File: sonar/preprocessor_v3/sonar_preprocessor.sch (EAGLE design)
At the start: 3 parts

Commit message: Worked on general board dimensions
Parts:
- removed PH1, PH2: PINHD-2X23_2.54, pinhead-1:PINHD-2X23_2.54
- added P8, P9: PINHD-2X23_2.54, pinhead-1:PINHD-2X23_2.54
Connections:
- new net DGND: P9.2

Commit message: Work on headers
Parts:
- removed P8, P9: PINHD-2X23_2.54, pinhead-1:PINHD-2X23_2.54
- added PH1, PH2: PINHD-2X23_2.54, pinhead-1:PINHD-2X23_2.54
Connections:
- removed net DGND: P9.2
- new net AIN0: PH2.39
- new net AIN1: PH2.40
- new net AIN2: PH2.37
- new net AIN3: PH2.38
- new net AIN4: PH2.33
- new net AIN5: PH2.36
- new net AIN6: PH2.35
- new net ECAPWMO: PH2.42
- new net EHRPPWM2A: PH1.19
- new net EHRPWM1A: PH2.14
- new net EHRPWM1B: PH2.16
- new net EHRPWM2B: PH1.13
- new net GND: JP2.1, PH1.1, PH1.2, PH2.1, PH2.2, PH2.43, PH2.44, PH2.45, PH2.46
- new net GND_ADC: PH2.34
- new net GPIO_112: PH2.30
- new net GPIO_115: PH2.27
- new net GPIO_117: PH2.25
- new net GPIO_20: PH2.41
- new net GPIO_26: PH1.14
- new net GPIO_27: PH1.17
- new net GPIO_44: PH1.12
- new net GPIO_45: PH1.11
- new net GPIO_46: PH1.16
- new net GPIO_47: PH1.15
- new net GPIO_48: PH2.15
- new net GPIO_49: PH2.23
- new net GPIO_60: PH2.12
- new net GPIO_61: PH1.26
- new net GPIO_65: PH1.18
- new net GPIO_66: PH1.7
- new net GPIO_67: PH1.8
- new net GPIO_68: PH1.10
- new net GPIO_69: PH1.9
- new net I2C_SCL: PH2.19
- new net I2C_SDA: PH2.20
- new net IN0: JP2.2
- new net IN1: JP2.4
- new net IN2: JP2.6
- new net IN3: JP2.8
- new net IN4: JP2.10
- new net LCD_AC_BIAS: PH1.30
- new net LCD_DATA0: PH1.45
- new net LCD_DATA1: PH1.46
- new net LCD_DATA10: PH1.36
- new net LCD_DATA11: PH1.34
- new net LCD_DATA12: PH1.35
- new net LCD_DATA13: PH1.33
- new net LCD_DATA14: PH1.31
- new net LCD_DATA15: PH1.32
- new net LCD_DATA2: PH1.43
- new net LCD_DATA3: PH1.44
- new net LCD_DATA4: PH1.41
- new net LCD_DATA5: PH1.42
- new net LCD_DATA6: PH1.39
- new net LCD_DATA7: PH1.40
- new net LCD_DATA8: PH1.37
- new net LCD_DATA9: PH1.38
- new net LCD_HSYNC: PH1.29
- new net LCD_PCLK: PH1.28
- new net LCD_VSYNC: PH1.27
- new net MMC1_CLK: PH1.21
- new net MMC1_CMD: PH1.20
- new net MMC1_DAT1: PH1.24
- new net MMC1_DAT2: PH1.5
- new net MMC1_DAT3: PH1.6
- new net MMC1_DAT4: PH1.23
- new net MMC1_DAT5: PH1.22
- new net MMC1_DAT6: PH1.3
- new net MMC1_DAT7: PH1.4
- new net MMC1_DATO: PH1.25
- new net PWR_BUT: PH2.9
- new net SP11_CLK: PH2.31
- new net SP11_CSO: PH2.28
- new net SP11_DO: PH2.29
- new net SPIO_CSO: PH2.17
- new net SPIO_D1: PH2.18
- new net SPIO_DO: PH2.21
- new net SPIO_SCLK: PH2.22
- new net SYS_5V: PH2.7, PH2.8
- new net SYS_RESET: PH2.10
- new net UART1_RXD: PH2.26
- new net UART1_TXD: PH2.24
- new net UART4_RXD: PH2.11
- new net UART4_TXD: PH2.13
- new net VDD_3V3: PH2.3, PH2.4
- new net VDD_5V: PH2.5, PH2.6
- new net VDD_ADC: PH2.32
- new net VREF: JP2.9

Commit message: Reworked board dimensions and mounting
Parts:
- removed JP2: (no value), pinhead:PINHD-2X5
- removed PH1, PH2: PINHD-2X23_2.54, pinhead-1:PINHD-2X23_2.54
- added C1, C3, C5: 100n, rcl:C-EUC0805
- added C10, C8, C9: (no value), Kondensatoren (rev17a):WCAP-AS5H_4X5,5_865230340001
- added C4, C6, C7: 1u, rcl:C-EUC0805
- added CON4: MOLEX_5566-2, ARVP:MOLEX_5566-2
- added JP1: (no value), pinhead:PINHD-1X5/90
- added R1, R10, R11, R2, R5, R6, R7, R8, R9: 25k, rcl:R-US_R0805
- added R3, R4: 10k, rcl:R-US_R0805
- added U1: TEENSY_3.1_BASIC, Teensy_3_Series_Board_v1.0:TEENSY_3.1_BASIC
- added U2: LTC6242, ARVP:LTC6242IGNPBFSSOP16
- added U3: REF3318AIDBZRSOT-23, ARVP:REF3318AIDBZRSOT-23
- added U4: TLV70018DDCRSOT-5, ARVP:TLV70018DDCRSOT-5
- added X1, X2, X3: BN35N61, con-coax:BN35N61
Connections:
- removed net AIN0: PH2.39
- removed net AIN1: PH2.40
- removed net AIN2: PH2.37
- removed net AIN3: PH2.38
- removed net AIN4: PH2.33
- removed net AIN5: PH2.36
- removed net AIN6: PH2.35
- removed net ECAPWMO: PH2.42
- removed net EHRPPWM2A: PH1.19
- removed net EHRPWM1A: PH2.14
- removed net EHRPWM1B: PH2.16
- removed net EHRPWM2B: PH1.13
- removed net GND_ADC: PH2.34
- removed net GPIO_112: PH2.30
- removed net GPIO_115: PH2.27
- removed net GPIO_117: PH2.25
- removed net GPIO_20: PH2.41
- removed net GPIO_26: PH1.14
- removed net GPIO_27: PH1.17
- removed net GPIO_44: PH1.12
- removed net GPIO_45: PH1.11
- removed net GPIO_46: PH1.16
- removed net GPIO_47: PH1.15
- removed net GPIO_48: PH2.15
- removed net GPIO_49: PH2.23
- removed net GPIO_60: PH2.12
- removed net GPIO_61: PH1.26
- removed net GPIO_65: PH1.18
- removed net GPIO_66: PH1.7
- removed net GPIO_67: PH1.8
- removed net GPIO_68: PH1.10
- removed net GPIO_69: PH1.9
- removed net IN0: JP2.2
- removed net IN1: JP2.4
- removed net IN2: JP2.6
- removed net IN3: JP2.8
- removed net IN4: JP2.10
- removed net LCD_AC_BIAS: PH1.30
- removed net LCD_DATA0: PH1.45
- removed net LCD_DATA1: PH1.46
- removed net LCD_DATA10: PH1.36
- removed net LCD_DATA11: PH1.34
- removed net LCD_DATA12: PH1.35
- removed net LCD_DATA13: PH1.33
- removed net LCD_DATA14: PH1.31
- removed net LCD_DATA15: PH1.32
- removed net LCD_DATA2: PH1.43
- removed net LCD_DATA3: PH1.44
- removed net LCD_DATA4: PH1.41
- removed net LCD_DATA5: PH1.42
- removed net LCD_DATA6: PH1.39
- removed net LCD_DATA7: PH1.40
- removed net LCD_DATA8: PH1.37
- removed net LCD_DATA9: PH1.38
- removed net LCD_HSYNC: PH1.29
- removed net LCD_PCLK: PH1.28
- removed net LCD_VSYNC: PH1.27
- removed net MMC1_CLK: PH1.21
- removed net MMC1_CMD: PH1.20
- removed net MMC1_DAT1: PH1.24
- removed net MMC1_DAT2: PH1.5
- removed net MMC1_DAT3: PH1.6
- removed net MMC1_DAT4: PH1.23
- removed net MMC1_DAT5: PH1.22
- removed net MMC1_DAT6: PH1.3
- removed net MMC1_DAT7: PH1.4
- removed net MMC1_DATO: PH1.25
- removed net PWR_BUT: PH2.9
- removed net SP11_CLK: PH2.31
- removed net SP11_CSO: PH2.28
- removed net SP11_DO: PH2.29
- removed net SPIO_CSO: PH2.17
- removed net SPIO_D1: PH2.18
- removed net SPIO_DO: PH2.21
- removed net SPIO_SCLK: PH2.22
- removed net SYS_5V: PH2.7, PH2.8
- removed net SYS_RESET: PH2.10
- removed net UART4_RXD: PH2.11
- removed net UART4_TXD: PH2.13
- removed net VDD_3V3: PH2.3, PH2.4
- removed net VDD_ADC: PH2.32
- removed net VREF: JP2.9
- new net +1V8: C3.1, C4.1, U2.V+, U4.OUT
- new net +3V3: R3.1, R4.1, U1.3.3V
- new net +5V: C1.1, C7.1, CON4G$1.S, U3.VIN, U4.EN, U4.IN
- new net 1V8_REF: C5.1, C6.1, R1.2, R6.2, R9.2, U3.VOUT
- new net BIASED_0: C8.1, R1.1, R2.2, R5.2
- new net BIASED_1: C9.1, R6.1, R7.2, R8.2
- new net BIASED_2: C10.1, R10.2, R11.2, R9.1
- new net CLAMP_IN_0: R5.1, U2.+INC
- new net CLAMP_IN_1: R8.1, U2.+IND
- new net CLAMP_IN_2: R11.1, U2.+INA
- new net FILTER_OUT_0: C8.2
- new net FILTER_OUT_1: C9.2
- new net FILTER_OUT_2: C10.2
- new net SIG_OUT_0: JP1.5, U2.-INC, U2.OUTC
- new net SIG_OUT_1: JP1.3, U2.-IND, U2.OUTD
- new net SIG_OUT_2: JP1.1, U2.-INA, U2.OUTA
- net GND: now also C1.2, C3.2, C4.2, C5.2, C6.2, C7.2, CON4G$2.S, JP1.2, JP1.4, R10.1, R2.1, R7.1, U1.AGND, U1.GND, U2.V-, U3.GND, U4.GND, U4.NC, X1.2, X2.2, X3.2; no longer JP2.1, PH1.1, PH1.2, PH2.1, PH2.2, PH2.43, PH2.44, PH2.45, PH2.46
- net I2C_SCL: now also R4.2, U1.19/A5/T/SCL0; no longer PH2.19
- net I2C_SDA: now also R3.2, U1.18/A4/T/SDA0; no longer PH2.20
- net UART1_RXD: now also U1.0/RX1/T; no longer PH2.26
- net UART1_TXD: now also U1.1/TX1/T; no longer PH2.24
- net VDD_5V: now also U1.VBAT; no longer PH2.5, PH2.6

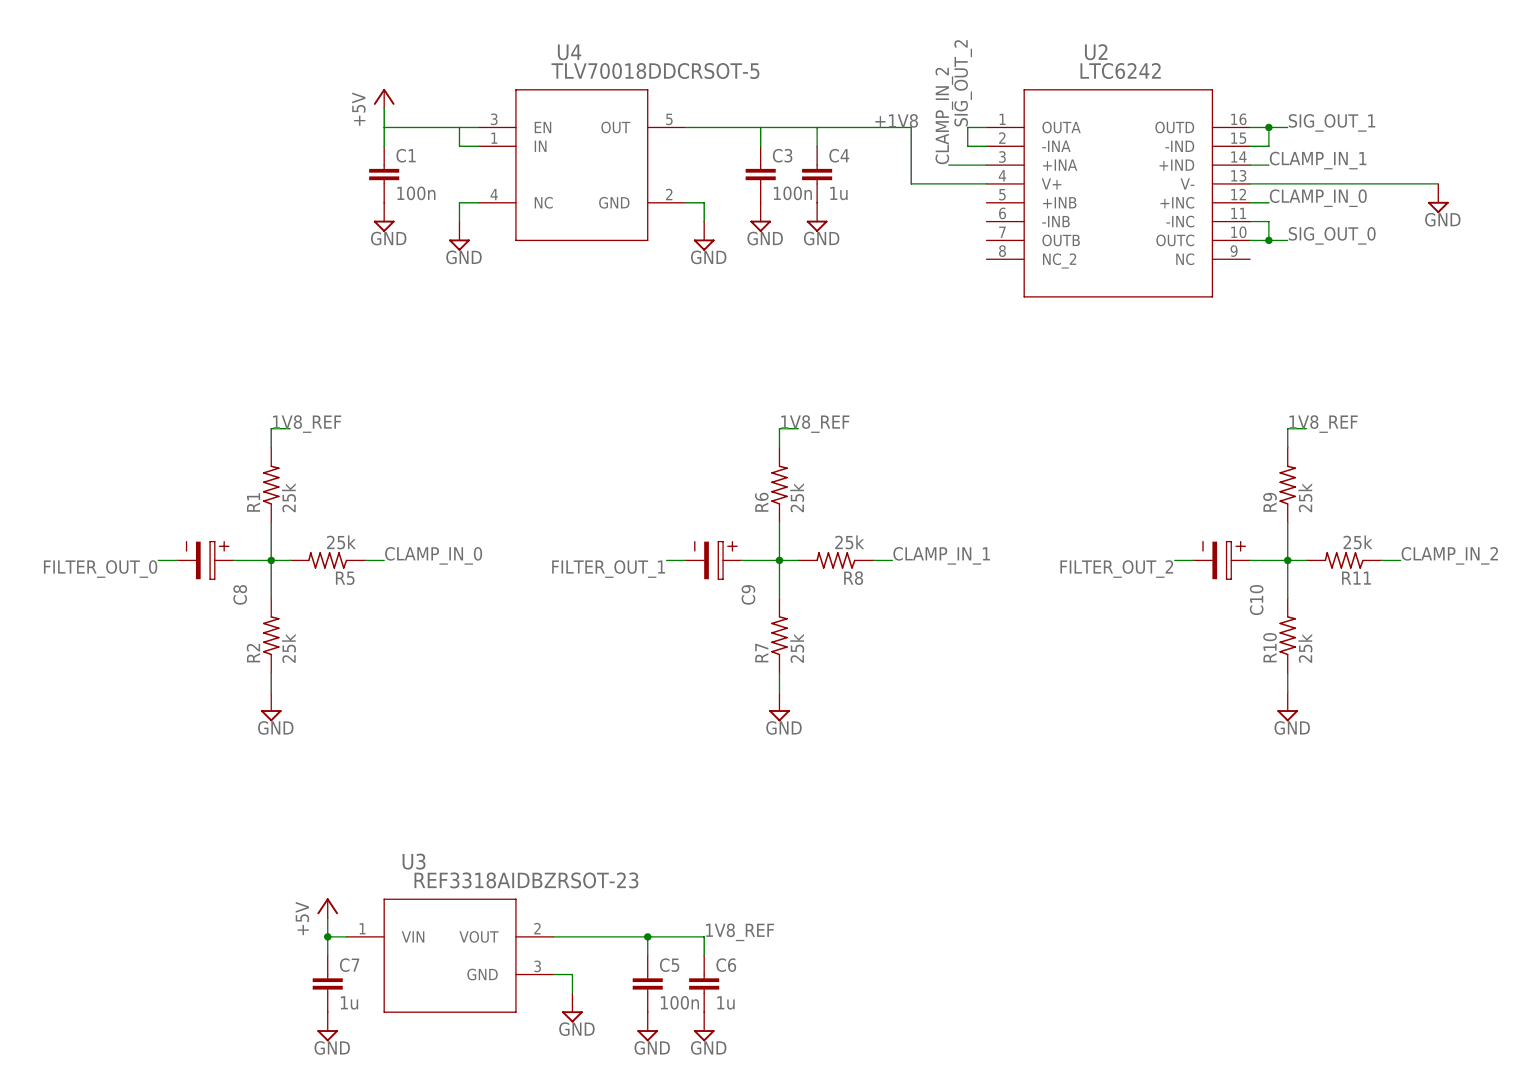
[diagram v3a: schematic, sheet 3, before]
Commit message: Bias/clamp work, overall layout work
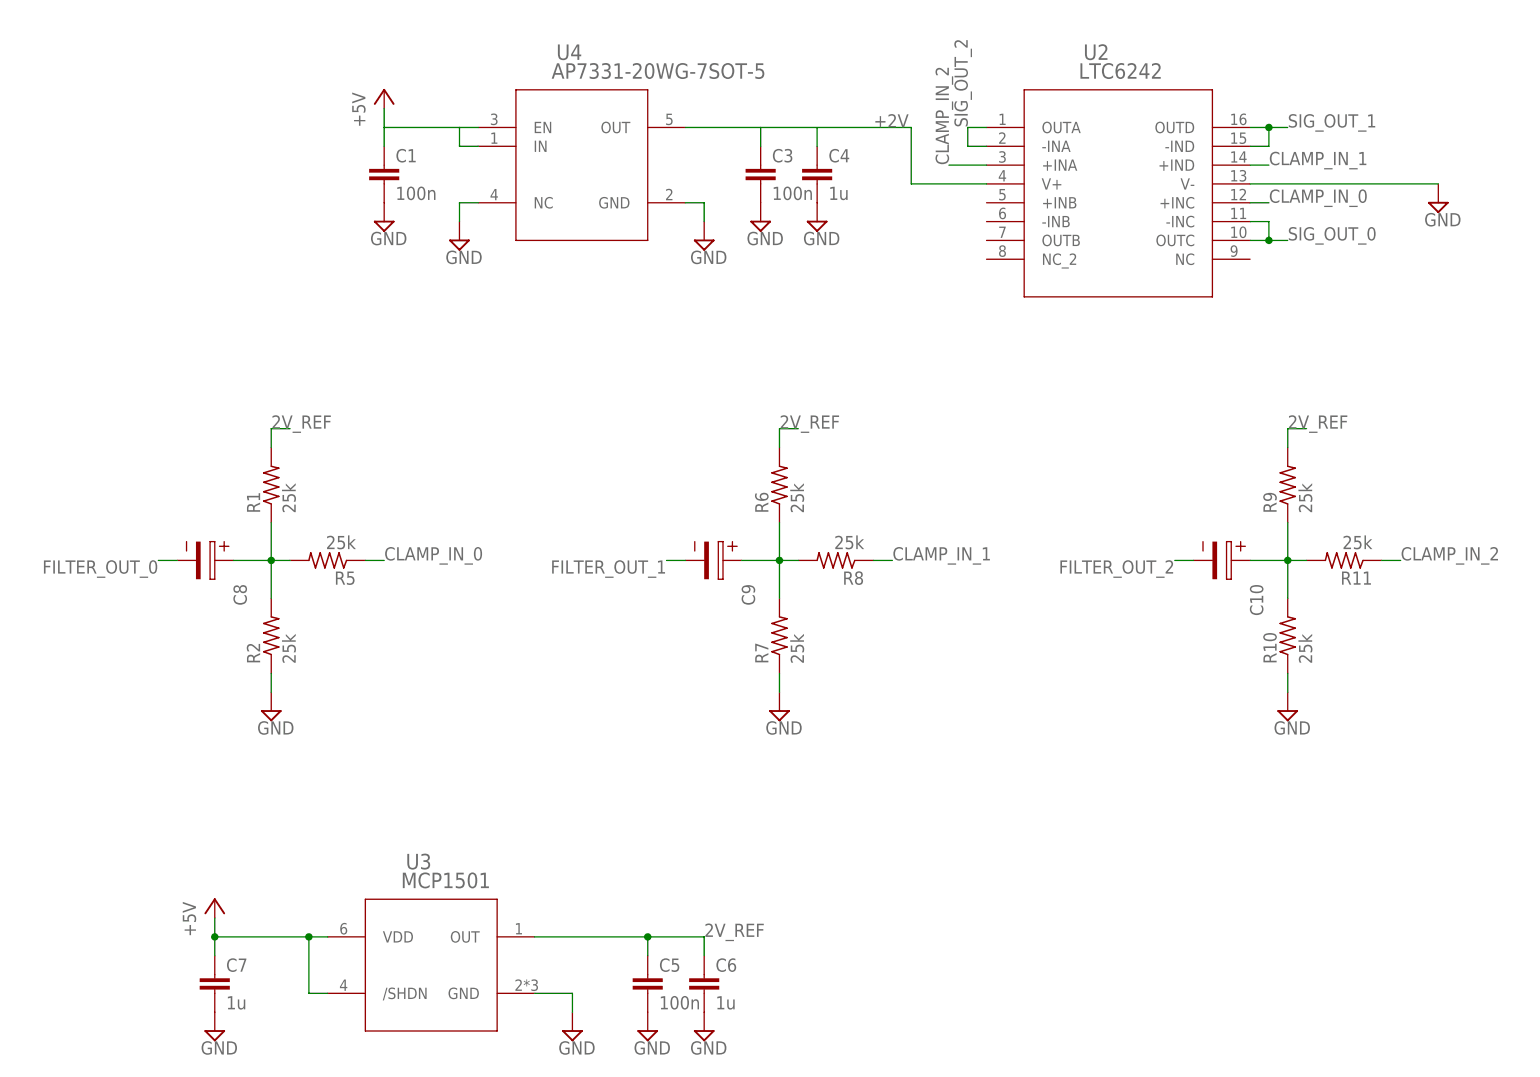
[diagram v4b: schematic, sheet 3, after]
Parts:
- U3: value REF3318AIDBZRSOT-23 -> MCP1501; device ARVP:REF3318AIDBZRSOT-23 -> ARVP:MCP1501
- U4: value TLV70018DDCRSOT-5 -> AP7331-20WG-7SOT-5; device ARVP:TLV70018DDCRSOT-5 -> ARVP:AP7331-20WG-7SOT-5
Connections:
- net +1V8 renamed +2V
- removed net 1V8_REF: C5.1, C6.1, R1.2, R6.2, R9.2, U3.VOUT
- new net 2V_REF: C5.1, C6.1, R1.2, R6.2, R9.2, U3.OUT
- net +5V: now also U3./SHDN, U3.VDD; no longer U3.VIN
- net GND: no longer U3.GND
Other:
- moved on the sheet: C7
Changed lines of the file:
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@@
 <?xml version="1.0" encoding="utf-8"?>
 <!DOCTYPE eagle SYSTEM "eagle.dtd">
-<eagle version="8.7.0">
+<eagle version="8.7.1">
 <drawing>
 <settings>
@@
 <part name="SUPPLY6" library="supply2" library_urn="urn:adsk.eagle:library:372" deviceset="GND" device=""/>
 <part name="U2" library="ARVP" deviceset="LTC6242IGNPBF" device="SSOP16" value="LTC6242"/>
-<part name="U3" library="ARVP" deviceset="REF3318AIDBZR" device="SOT-23" value="REF3318AIDBZRSOT-23"/>
-<part name="U4" library="ARVP" deviceset="TLV70018DDCR" device="SOT-5"/>
+<part name="U4" library="ARVP" deviceset="AP7331-20WG-7" device="SOT-5"/>
 <part name="SUPPLY7" library="supply2" library_urn="urn:adsk.eagle:library:372" deviceset="GND" device=""/>
 <part name="SUPPLY8" library="supply2" library_urn="urn:adsk.eagle:library:372" deviceset="GND" device=""/>
@@
 <part name="JP1" library="pinhead" library_urn="urn:adsk.eagle:library:325" deviceset="PINHD-1X5" device="/90" package3d_urn="urn:adsk.eagle:package:22467/2"/>
 <part name="SUPPLY11" library="supply2" library_urn="urn:adsk.eagle:library:372" deviceset="GND" device=""/>
+<part name="U3" library="ARVP" deviceset="MCP1501" device=""/>
 </parts>
 <sheets>
@@
 <instance part="FRAME2" gate="G$1" x="0" y="0"/>
 <instance part="U2" gate="A" x="147.32" y="147.32"/>
-<instance part="U3" gate="A" x="60.96" y="38.1"/>
 <instance part="U4" gate="A" x="78.74" y="147.32"/>
 <instance part="SUPPLY7" gate="GND" x="210.82" y="137.16"/>
@@
 <instance part="SUPPLY12" gate="GND" x="119.38" y="134.62"/>
 <instance part="SUPPLY13" gate="GND" x="127" y="134.62"/>
-<instance part="SUPPLY14" gate="GND" x="93.98" y="27.94"/>
+<instance part="SUPPLY14" gate="GND" x="93.98" y="25.4"/>
 <instance part="C5" gate="G$1" x="104.14" y="33.02"/>
 <instance part="C6" gate="G$1" x="111.76" y="33.02"/>
 <instance part="SUPPLY15" gate="GND" x="104.14" y="25.4"/>
 <instance part="SUPPLY16" gate="GND" x="111.76" y="25.4"/>
-<instance part="P+3" gate="1" x="60.96" y="43.18"/>
-<instance part="C7" gate="G$1" x="60.96" y="33.02"/>
-<instance part="SUPPLY17" gate="GND" x="60.96" y="25.4"/>
+<instance part="P+3" gate="1" x="45.72" y="43.18"/>
+<instance part="C7" gate="G$1" x="45.72" y="33.02"/>
+<instance part="SUPPLY17" gate="GND" x="45.72" y="25.4"/>
 <instance part="C8" gate="G$1" x="43.18" y="88.9" rot="R270"/>
 <instance part="R1" gate="G$1" x="53.34" y="99.06" rot="R90"/>
@@
 <instance part="SUPPLY20" gate="GND" x="190.5" y="68.58"/>
 <instance part="R11" gate="G$1" x="198.12" y="88.9" rot="R180"/>
+<instance part="U3" gate="G$1" x="58.42" y="38.1"/>
 </instances>
 <busses>
@@
 </segment>
 <segment>
-<pinref part="U3" gate="A" pin="GND"/>
 <pinref part="SUPPLY14" gate="GND" pin="GND"/>
-<wire x1="91.44" y1="33.02" x2="93.98" y2="33.02" width="0.1524" layer="91"/>
-<wire x1="93.98" y1="33.02" x2="93.98" y2="30.48" width="0.1524" layer="91"/>
+<wire x1="88.9" y1="30.48" x2="93.98" y2="30.48" width="0.1524" layer="91"/>
+<wire x1="93.98" y1="30.48" x2="93.98" y2="27.94" width="0.1524" layer="91"/>
 </segment>
 <segment>
@@
 </segment>
 </net>
-<net name="+1V8" class="0">
+<net name="+2V" class="0">
 <segment>
 <pinref part="U4" gate="A" pin="OUT"/>
@@
 </segment>
 <segment>
-<pinref part="U3" gate="A" pin="VIN"/>
-<wire x1="63.5" y1="38.1" x2="60.96" y2="38.1" width="0.1524" layer="91"/>
-<wire x1="60.96" y1="38.1" x2="60.96" y2="40.64" width="0.1524" layer="91"/>
 <pinref part="P+3" gate="1" pin="+5V"/>
 <pinref part="C7" gate="G$1" pin="1"/>
-<wire x1="60.96" y1="35.56" x2="60.96" y2="38.1" width="0.1524" layer="91"/>
-<junction x="60.96" y="38.1"/>
+<wire x1="45.72" y1="35.56" x2="45.72" y2="38.1" width="0.1524" layer="91"/>
+<pinref part="U3" gate="G$1" pin="VDD"/>
+<wire x1="45.72" y1="38.1" x2="45.72" y2="40.64" width="0.1524" layer="91"/>
+<wire x1="45.72" y1="38.1" x2="58.42" y2="38.1" width="0.1524" layer="91"/>
+<wire x1="58.42" y1="38.1" x2="60.96" y2="38.1" width="0.1524" layer="91"/>
+<wire x1="58.42" y1="38.1" x2="58.42" y2="30.48" width="0.1524" layer="91"/>
+<pinref part="U3" gate="G$1" pin="/SHDN"/>
+<wire x1="58.42" y1="30.48" x2="60.96" y2="30.48" width="0.1524" layer="91"/>
+<junction x="45.72" y="38.1"/>
+<junction x="58.42" y="38.1"/>
 </segment>
 </net>
@@
 </segment>
 </net>
-<net name="1V8_REF" class="0">
+<net name="2V_REF" class="0">
 <segment>
 <pinref part="C5" gate="G$1" pin="1"/>
@@
 <pinref part="C6" gate="G$1" pin="1"/>
 <wire x1="111.76" y1="35.56" x2="111.76" y2="38.1" width="0.1524" layer="91"/>
-<pinref part="U3" gate="A" pin="VOUT"/>
-<wire x1="91.44" y1="38.1" x2="104.14" y2="38.1" width="0.1524" layer="91"/>
+<wire x1="88.9" y1="38.1" x2="104.14" y2="38.1" width="0.1524" layer="91"/>
 <wire x1="104.14" y1="38.1" x2="111.76" y2="38.1" width="0.1524" layer="91"/>
 <junction x="104.14" y="38.1"/>
 <label x="111.76" y="38.1" size="1.778" layer="95"/>
-</segment>
-<segment>
+<pinref part="U3" gate="G$1" pin="OUT"/>
+</segment>
+<segment>
